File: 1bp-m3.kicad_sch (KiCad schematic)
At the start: 5 parts, among them J1 TCS7913-43, P13 TP_50, P7 TP_50, P8 TP_50, P9 TP_50

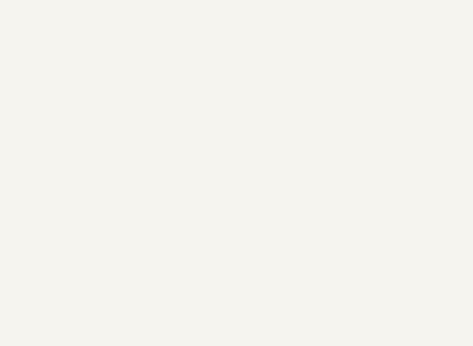
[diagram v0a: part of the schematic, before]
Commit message: updated silkscreen for OSHW
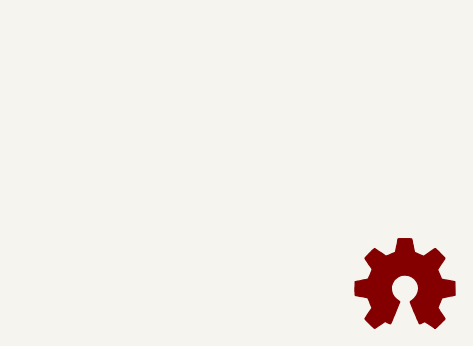
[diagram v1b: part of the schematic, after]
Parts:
- added LOGO1: Logo_Open_Hardware_Small, Symbol:OSHW-Logo2_7.3x6mm_SilkScreen, symbol Graphic:Logo_Open_Hardware_Small
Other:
- title: Genesis Single Bypass Model 3 -> Genesis Model 3 Stereo Audio
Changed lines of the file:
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@@
   (paper "A")
   (title_block
-    (title "Genesis Single Bypass Model 3")
+    (title "Genesis Model 3 Stereo Audio")
     (date "2021-01-17")
     (rev "A")
     (company "Late to the Game")
-    (comment 1 "https://github.com/LateToTheGame16/sega-triple-bypass")
+    (comment 1 "https://github.com/LateToTheGame16/Genesis-Model3-Stereo")
     (comment 2 "Licensed under CERN OHL v.1.2")
     (comment 3 "For Genesis 3 consoles only")
@@
     (pin "1")
   )
+  (symbol (lib_id "Graphic:Logo_Open_Hardware_Small") (at 254 180.34 0) (unit 1)
+    (in_bom yes) (on_board yes) (fields_autoplaced)
+    (property "Reference" "LOGO1" (id 0) (at 254 173.355 0)
+      (effects (font (size 1.27 1.27)) hide)
+    )
+    (property "Value" "Logo_Open_Hardware_Small" (id 1) (at 254 186.055 0)
+      (effects (font (size 1.27 1.27)) hide)
+    )
+    (property "Footprint" "Symbol:OSHW-Logo2_7.3x6mm_SilkScreen" (id 2) (at 254 180.34 0)
+      (effects (font (size 1.27 1.27)) hide)
+    )
+    (property "Datasheet" "~" (id 3) (at 254 180.34 0)
+      (effects (font (size 1.27 1.27)) hide)
+    )
+  )
   (sheet (at 104.14 90.17) (size 40.64 27.94) (fields_autoplaced)
     (stroke (width 0) (type solid) (color 0 0 0 0))
@@
       (reference "J1") (unit 1) (value "TCS7913-43") (footprint "footprints:MiniDIN_TCS7913-43")
     )
+    (path "/bef3bb41-5dd6-4e07-9e39-f128ef5b94e9"
+      (reference "LOGO1") (unit 1) (value "Logo_Open_Hardware_Small") (footprint "Symbol:OSHW-Logo2_7.3x6mm_SilkScreen")
+    )
     (path "/00000000-0000-0000-0000-00005c1fe7d9"

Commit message: export gerbers
first fab run
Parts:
- LOGO1: now left out of the parts list
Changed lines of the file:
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@@
   )
   (symbol (lib_id "Graphic:Logo_Open_Hardware_Small") (at 254 180.34 0) (unit 1)
-    (in_bom yes) (on_board yes) (fields_autoplaced)
+    (in_bom no) (on_board yes) (fields_autoplaced)
     (property "Reference" "LOGO1" (id 0) (at 254 173.355 0)
       (effects (font (size 1.27 1.27)) hide)

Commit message: Saved in KiCad 8.0, fixed part descriptions
Component descriptions were wrong. Parts said 0603 but were really a 0402 footprint. No real changes to schematic or pcb. Saving from KiCad 6 to KiCad 8 created lots of format changes.
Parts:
- J1, LOGO1: now not fitted
- P13, P7, P8, P9: Digikey #ND -> (none); now not fitted
